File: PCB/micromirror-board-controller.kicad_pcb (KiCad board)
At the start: 2 copper layers, 65 x 30 mm, 22 parts, among them J1 RPi header, J2 Conn_01x04_Female, J3 Conn_01x03_Female, J4 51-pin conn, J5 Barrel_Jack, J7 5V Ext, J8 Conn_01x04_Socket

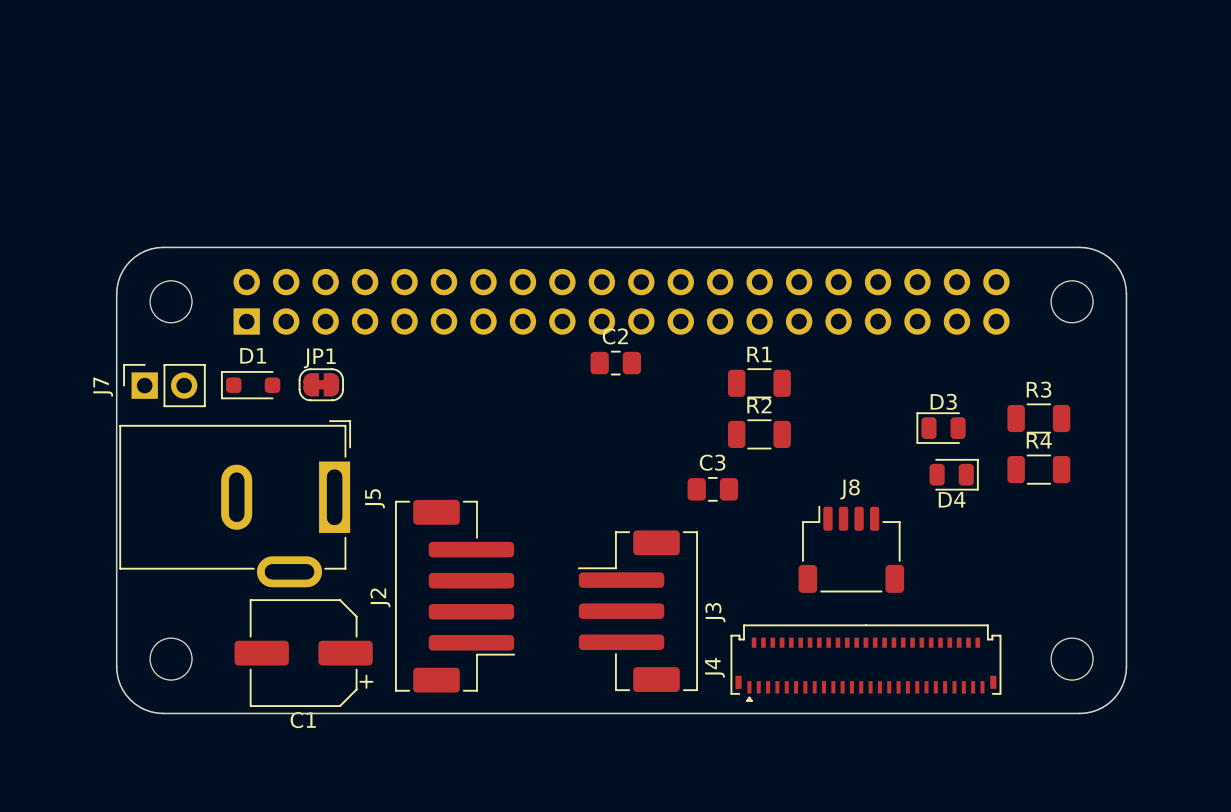
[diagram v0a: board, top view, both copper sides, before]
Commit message: functional parallel routing
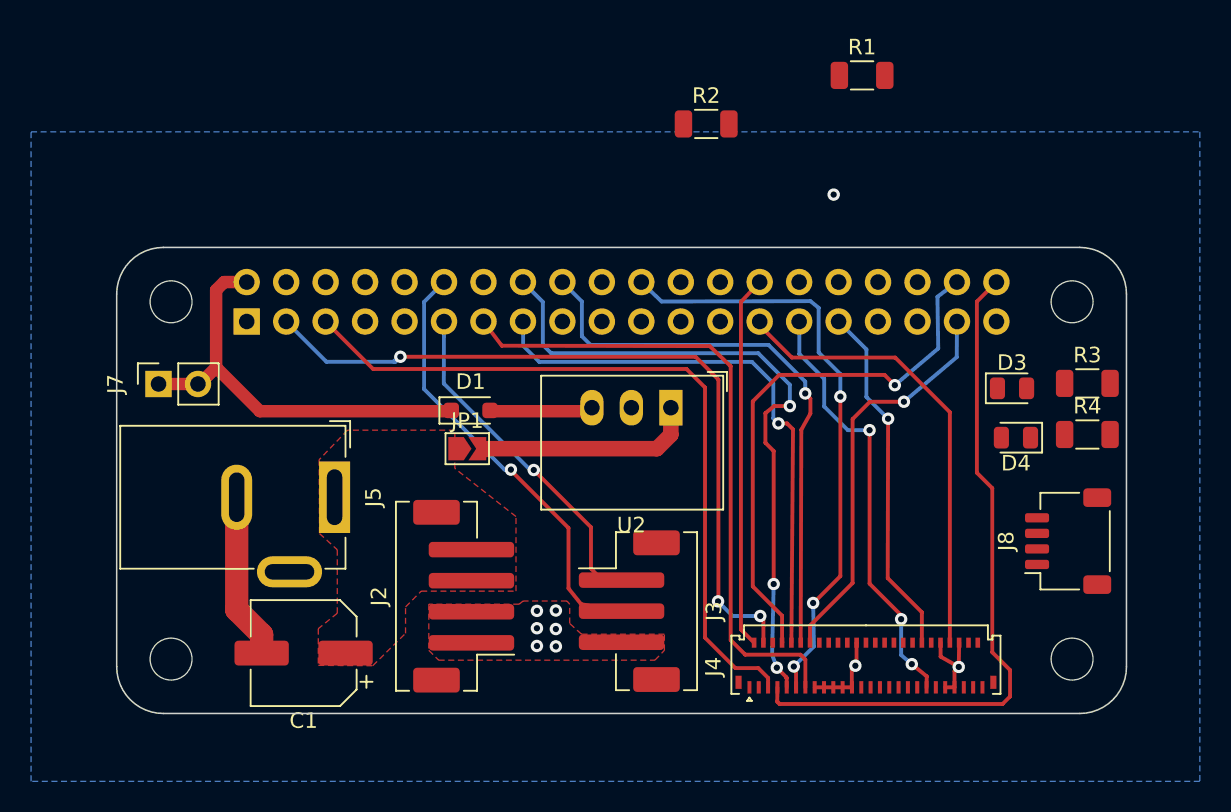
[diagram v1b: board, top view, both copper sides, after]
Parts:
- removed C2, C3: 10uF, Capacitor_SMD:C_0805_2012Metric_Pad1.18x1.45mm_HandSolder
- added U2: CUI P78E05-1000, Converter_DCDC:Converter_DCDC_RECOM_R-78E-0.5_THT, F.Cu at (135.7, 80.3)
- J2: value Conn_01x04_Female -> DMD board PWR
- JP1: footprint Jumper:SolderJumper-2_P1.3mm_Bridged_RoundedPad1.0x1.5mm -> Jumper:SolderJumper-2_P1.3mm_Open_TrianglePad1.0x1.5mm
- moved R1 20.9 mm to (148.0, 58.9)
- moved R2 20.3 mm to (137.9, 62.1)
- moved D1 14.1 mm to (122.8, 80.5)
- moved J8 14.0 mm to (161.2, 88.9), turned to 90 degrees
- moved JP1 10.3 mm to (122.6, 83.0)
- moved D3 5.10 mm to (157.6, 79.1)
- moved D4 4.78 mm to (157.9, 82.2)
- moved R4 3.85 mm to (162.5, 82.0)
- moved R3 3.85 mm to (162.5, 78.8)
- moved J7 0.89 mm to (102.7, 78.8)
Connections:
- D1 pad 1: /+5V VSYS -> +5V
- D1 pad 2: /+5V -> /5V_raw
- J1 pad 1: +3.3V -> unconnected-(J1-Pin_1-Pad1)
- J1 pad 11: unconnected-(J1-Pin_11-Pad11) -> SDA
- J1 pad 12: unconnected-(J1-Pin_12-Pad12) -> SCL
- J1 pad 14: unconnected-(J1-Pin_14-Pad14) -> GND
- J1 pad 17: unconnected-(J1-Pin_17-Pad17) -> +3.3V
- J1 pad 2: unconnected-(J1-Pin_2-Pad2) -> +5V
- J1 pad 20: unconnected-(J1-Pin_20-Pad20) -> GND
- J1 pad 21: SCL -> unconnected-(J1-Pin_21-Pad21)
- J1 pad 23: SDA -> unconnected-(J1-Pin_23-Pad23)
- J1 pad 25: unconnected-(J1-Pin_25-Pad25) -> GND
- J1 pad 30: unconnected-(J1-Pin_30-Pad30) -> GND
- J1 pad 34: unconnected-(J1-Pin_34-Pad34) -> GND
- J1 pad 39: unconnected-(J1-Pin_39-Pad39) -> GND
- J1 pad 4: unconnected-(J1-Pin_4-Pad4) -> +5V
- J1 pad 6: unconnected-(J1-Pin_6-Pad6) -> GND
- J1 pad 9: unconnected-(J1-Pin_9-Pad9) -> GND
- J3 pad 2: SCl -> SCL
- J7 pad 1: /+5V VSYS -> +5V
- J7 pad 2: /+5V VSYS -> +5V
- J8 pad 1: SCl -> SCL
- JP1 pad 1: /+5V -> /+12V
- JP1 pad 2: /+5V -> /+12V
- R1 pad 1: SCl -> SCL
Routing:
- net /Vsync: track 0.00 -> 49.6 mm, vias 0 -> 3
- net /Hsync: track 0.00 -> 47.6 mm
- net P1: track 0.00 -> 44.3 mm
- net P3: track 0.00 -> 42.9 mm, vias 0 -> 3
- net P7: track 0.00 -> 42.0 mm
- net P5: track 0.00 -> 38.6 mm, vias 0 -> 3
- net P4: track 0.00 -> 36.7 mm, vias 0 -> 1
- net P2: track 0.00 -> 36.2 mm, vias 0 -> 1
- net P0: track 0.00 -> 35.1 mm, vias 0 -> 1
- net /PCLK: track 0.00 -> 29.7 mm
- net SCL: track 0.00 -> 28.3 mm, vias 0 -> 1
- net /PROJ_ON: track 0.00 -> 28.0 mm, vias 0 -> 3
- net +5V: track 0.00 -> 27.6 mm
- net P6: track 0.00 -> 26.1 mm, vias 0 -> 1
- net /DATAEN_CMD: track 0.00 -> 24.0 mm
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- added copper zone on F.Cu, net /+12V
- added copper zone on B.Cu, net GND
- added copper zone on F.Cu, net GND

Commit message: Completed routing and schematic
Did all the routing for the board. Schematic also close to final.
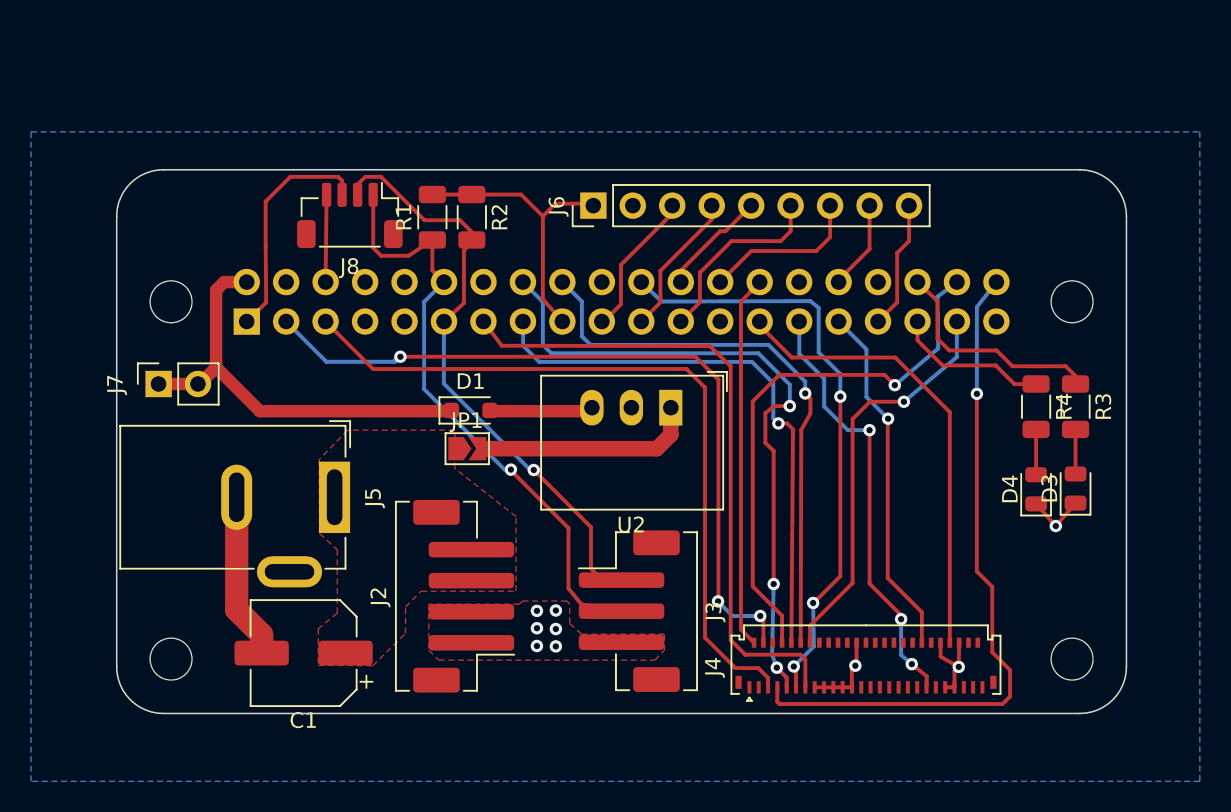
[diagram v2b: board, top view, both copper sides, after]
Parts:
- added J6: Extra GPIO, Connector_PinHeader_2.54mm:PinHeader_1x09_P2.54mm_Vertical, F.Cu at (130.7, 67.3)
- J8: value Conn_01x04_Socket -> STEMMA; footprint Connector_JST:JST_SH_SM04B-SRSS-TB_1x04-1MP_P1.00mm_Horizontal -> Connector_JST:JST_SH_BM04B-SRSS-TB_1x04-1MP_P1.00mm_Vertical
- moved J8 50.8 mm to (115.0, 67.9), turned to 180 degrees
- moved R1 29.1 mm to (120.3, 68.1), turned to 90 degrees
- moved R2 16.2 mm to (122.9, 68.1), turned to -90 degrees
- moved D3 7.64 mm to (161.7, 85.5), turned to 90 degrees
- moved R4 3.75 mm to (159.2, 80.3), turned to -90 degrees
- moved D4 3.57 mm to (159.2, 85.6), turned to 90 degrees
- moved R3 1.68 mm to (161.7, 80.3), turned to -90 degrees
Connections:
- J1 pad 1: unconnected-(J1-Pin_1-Pad1) -> +3.3V
- J1 pad 19: unconnected-(J1-Pin_19-Pad19) -> GPIO10
- J1 pad 21: unconnected-(J1-Pin_21-Pad21) -> GPIO9
- J1 pad 23: unconnected-(J1-Pin_23-Pad23) -> GPIO11
- J1 pad 24: unconnected-(J1-Pin_24-Pad24) -> GPIO8
- J1 pad 26: unconnected-(J1-Pin_26-Pad26) -> GPIO7
- J1 pad 32: unconnected-(J1-Pin_32-Pad32) -> GPIO12
- J1 pad 33: LED-G -> GPIO13
- J1 pad 36: unconnected-(J1-Pin_36-Pad36) -> LED-G
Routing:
- net +3.3V: track 0.00 -> 33.4 mm
- net SDA: track 22.2 -> 38.4 mm
- net LED-G: track 0.00 -> 14.6 mm
- net GPIO11: track 0.00 -> 12.2 mm
- net SCL: track 28.3 -> 39.0 mm
- net GPIO7: track 0.00 -> 10.3 mm
- net LED-R: track 0.00 -> 10.0 mm
- net GND: track 21.9 -> 31.4 mm, vias 8 -> 9
- net GPIO10: track 0.00 -> 9.41 mm
- net GPIO9: track 0.00 -> 9.34 mm
- net GPIO13: track 0.00 -> 8.28 mm
- net GPIO8: track 0.00 -> 7.00 mm
- net GPIO12: track 0.00 -> 5.75 mm
- net Net-(D4-A): track 0.00 -> 2.92 mm
- net Net-(D3-A): track 0.00 -> 2.87 mm
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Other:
- board size 65 x 30 mm -> 65 x 35 mm

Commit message: Added board silkscreen
Added proper pin labels and project graphics
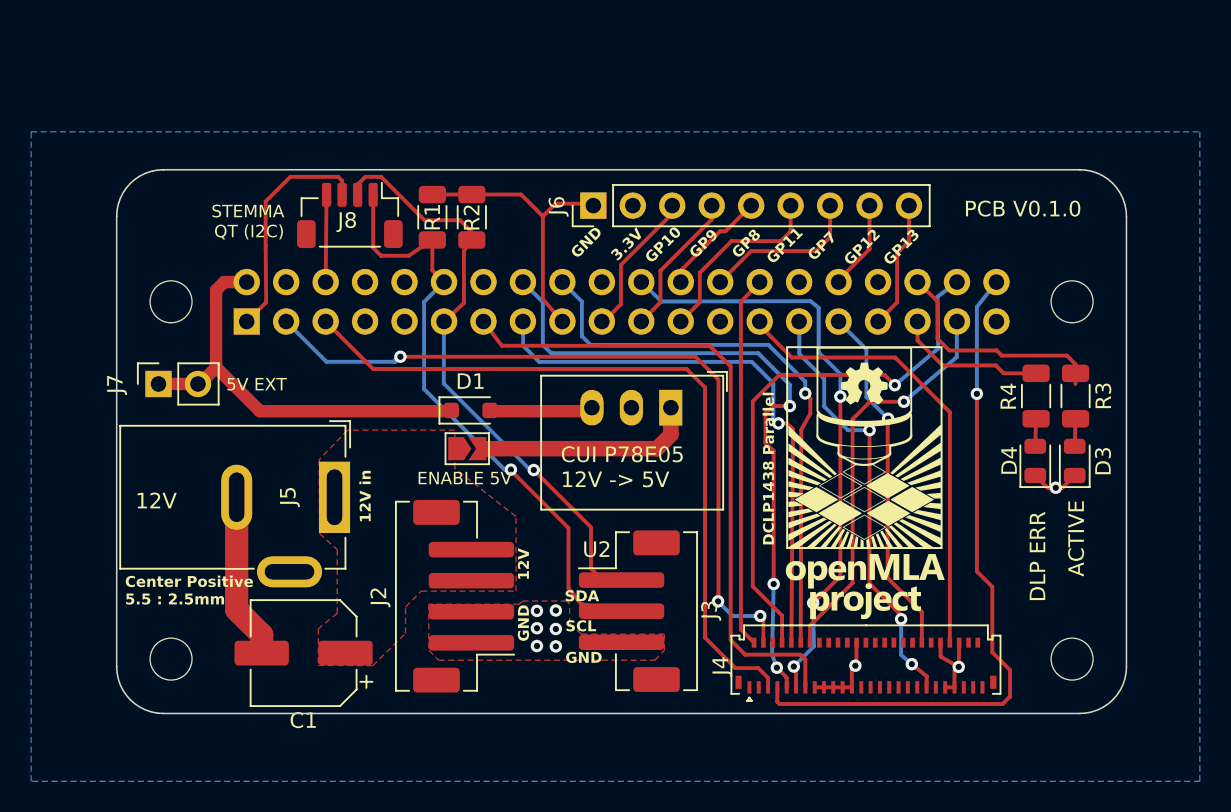
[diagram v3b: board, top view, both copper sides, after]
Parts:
- added G***: LOGO, board-assets:openMLA-logo-small, F.Cu at (148.1, 85.2)
- added G***: LOGO, board-assets:openMLA-logo, B.Cu at (134.5, 88.3)
- moved D4 1.83 mm to (159.1, 83.7)
- moved D3 1.78 mm to (161.7, 83.7)
- moved R3 0.69 mm to (161.7, 79.6)
- moved R4 0.69 mm to (159.2, 79.6)
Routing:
- net Net-(D4-A): track 2.92 -> 1.77 mm
- net Net-(D3-A): track 2.87 -> 1.77 mm
- net GND: track 31.4 -> 30.7 mm
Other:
- board text added: "12V"
- board text added: "12V in"
- board text added: "3.3V"
- board text added: "5V EXT"
- board text added: "ACTIVE"
- board text added: "CUI P78E05 12V -> 5V"
- board text added: "Center Positive 5.5 : 2.5mm"
- board text added: "DCLP1438 Parallel"
- board text added: "DLP ERR"
- board text added: "ENABLE 5V"
- board text added: "GND"
- board text added: "GP10"
- board text added: "GP11"
- board text added: "GP12"
- board text added: "GP13"
- board text added: "GP7"
- board text added: "GP8"
- board text added: "GP9"
- board text added: "PCB V0.1.0"
- board text added: "SCL"
- board text added: "SDA"
- board text added: "STEMMA QT (I2C)"
